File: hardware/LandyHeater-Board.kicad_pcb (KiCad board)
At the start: 4 copper layers, 98 x 48 mm, 0 parts

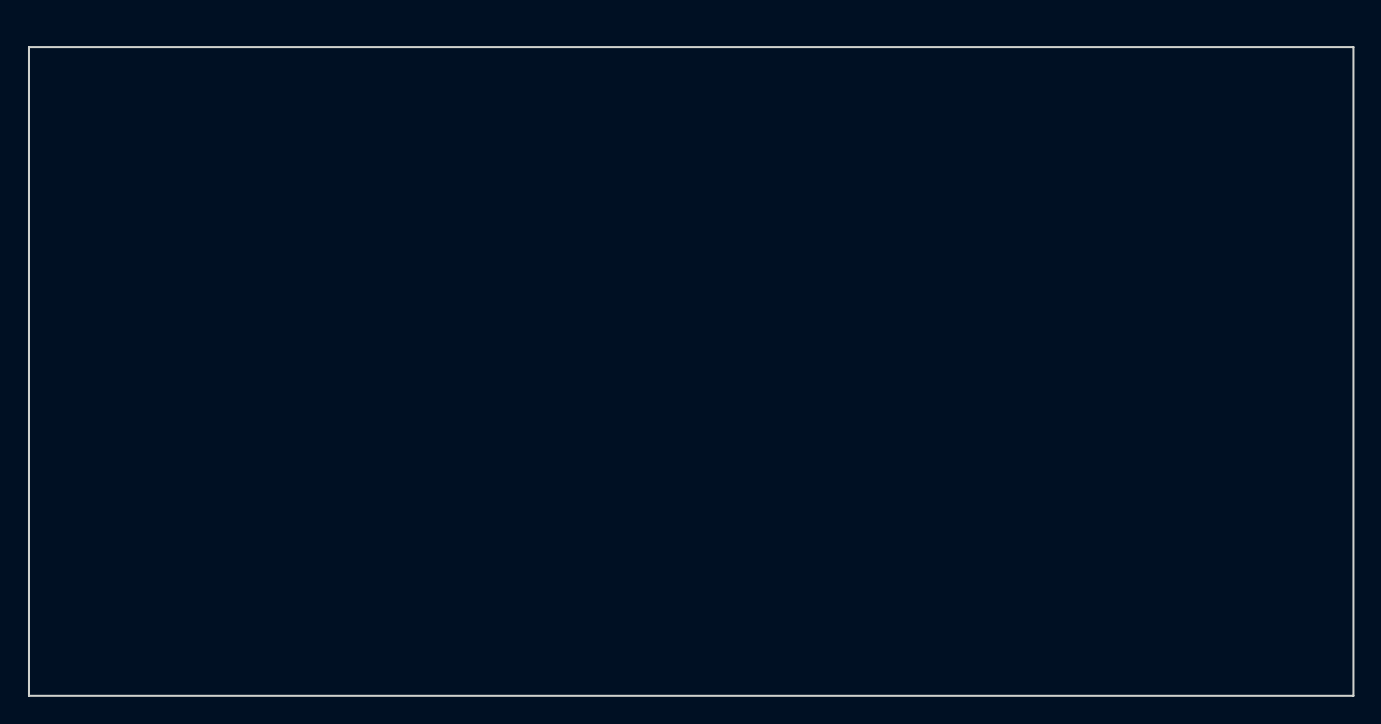
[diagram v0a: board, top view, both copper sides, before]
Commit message: Place Rev A board: 4-layer stackup, zones, two-sided placement
Generated by scripts/rebuild/gen_pcb.py from the same circuit definition.
Pre-route DRC: 0 errors, schematic parity: 0 issues.

Co-Authored-By: Claude Opus 5.5 <noreply@anthropic.com>
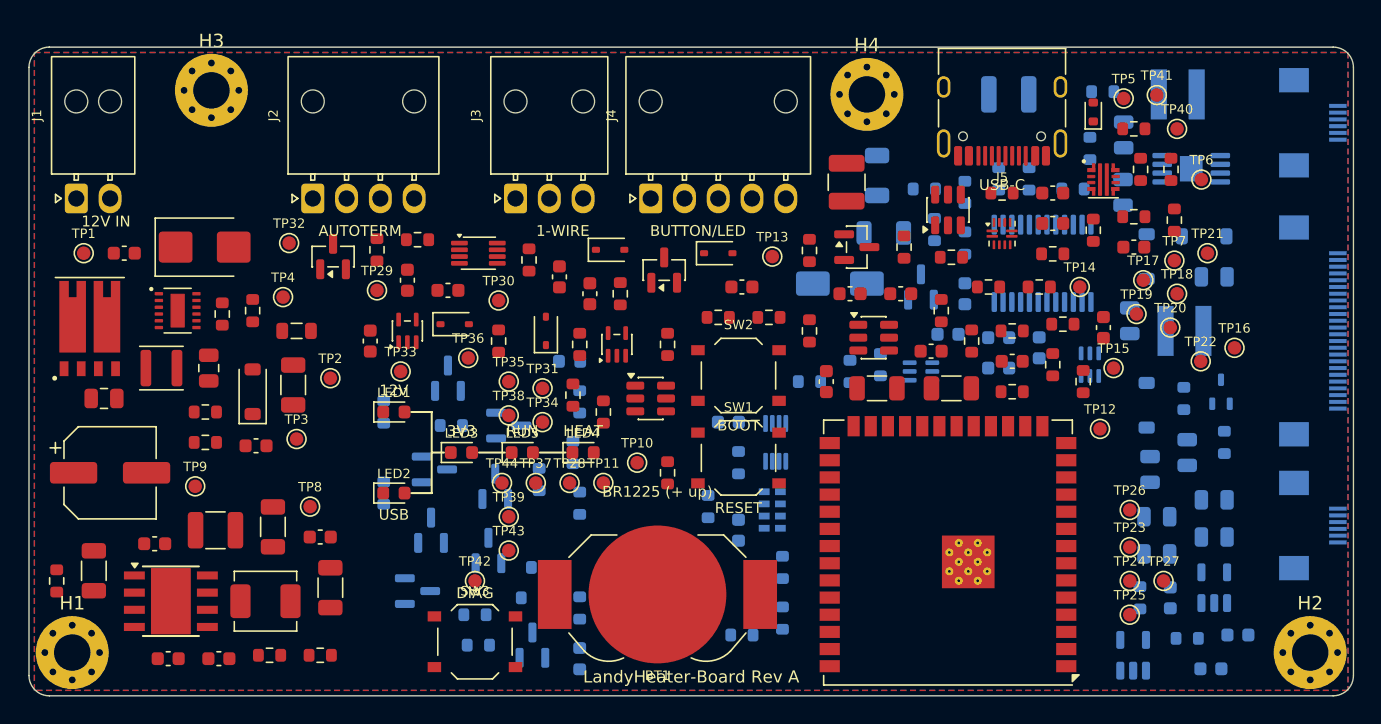
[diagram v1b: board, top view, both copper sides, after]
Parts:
- added BT1: BR1225, Battery:BatteryHolder_LINX_BAT-HLD-012-SMT, F.Cu at (146.5, 140.5)
- added C1: 100nF 50V X7R, Capacitor_SMD:C_0603_1608Metric, F.Cu at (107.0, 115.2)
- added C10: 4.7µF 50V X7R, Capacitor_SMD:C_1210_3225Metric, F.Cu at (113.8, 135.8)
- added C11: 4.7µF 50V X7R, Capacitor_SMD:C_1206_3216Metric, F.Cu at (104.8, 138.8)
- added C12: 100nF 50V X7R, Capacitor_SMD:C_0603_1608Metric, F.Cu at (109.3, 136.8)
- added C13: 100nF 50V X7R, Capacitor_SMD:C_0603_1608Metric, F.Cu at (114.0, 145.2)
- added C14: 1µF 50V X5R, Capacitor_SMD:C_0603_1608Metric, F.Cu at (110.3, 145.2)
- added C15: CFF opt., Capacitor_SMD:C_0603_1608Metric, F.Cu at (121.5, 136.2)
- added C16: 22µF 10V X7R, Capacitor_SMD:C_1206_3216Metric, F.Cu at (118.0, 135.5)
- added C17: 22µF 10V X7R, Capacitor_SMD:C_1206_3216Metric, F.Cu at (122.3, 140.0)
- added C18: 22µF 10V X7R, Capacitor_SMD:C_1206_3216Metric, F.Cu at (162.8, 125.2)
- added C19: 22µF 10V X7R, Capacitor_SMD:C_1206_3216Metric, F.Cu at (168.2, 125.2)
- added C2: 1µF 50V X7R, Capacitor_SMD:C_0805_2012Metric, F.Cu at (105.5, 126.0)
- added C20: 100nF 50V X7R, Capacitor_SMD:C_0603_1608Metric, F.Cu at (159.0, 124.8)
- added C21: 100nF 50V X7R, Capacitor_SMD:C_0603_1608Metric, F.Cu at (166.8, 122.5)
- added C22: 1µF 50V X5R, Capacitor_SMD:C_0603_1608Metric, F.Cu at (172.8, 123.2)
- added C23: 10pF C0G, Capacitor_SMD:C_0603_1608Metric, F.Cu at (164.5, 118.2)
- added C24: 10pF C0G, Capacitor_SMD:C_0603_1608Metric, F.Cu at (160.8, 118.2)
- added C25: 10pF C0G, Capacitor_SMD:C_0603_1608Metric, F.Cu at (179.5, 120.8)
- added C26: 1µF 50V X5R, Capacitor_SMD:C_0603_1608Metric, B.Cu at (169.2, 118.2)
- added C27: 100nF 50V X7R, Capacitor_SMD:C_0603_1608Metric, B.Cu at (171.8, 121.5)
- added C28: 100nF 50V X7R, Capacitor_SMD:C_0603_1608Metric, B.Cu at (168.0, 121.2)
- added C29: 100nF 50V X7R, Capacitor_SMD:C_0603_1608Metric, B.Cu at (174.8, 122.2)
- added C3: 1µF 50V X7R, Capacitor_SMD:C_0805_2012Metric, F.Cu at (113.3, 123.8)
- added C30: 100nF 50V X7R, Capacitor_SMD:C_0603_1608Metric, B.Cu at (171.8, 123.8)
- added C31: 4.7µF 25V X5R, Capacitor_SMD:C_0805_2012Metric, B.Cu at (187.7, 117.0)
- added C32: 4.7µF 25V X5R, Capacitor_SMD:C_0805_2012Metric, B.Cu at (185.7, 130.0)
- added C33: 1µF 50V X7R, Capacitor_SMD:C_0805_2012Metric, B.Cu at (181.4, 120.2)
- added C34: 1µF 50V X7R, Capacitor_SMD:C_0805_2012Metric, B.Cu at (187.7, 133.5)
- added C35: 1µF 50V X7R, Capacitor_SMD:C_0805_2012Metric, B.Cu at (182.9, 131.2)
- added C36: 1µF 50V X7R, Capacitor_SMD:C_0805_2012Metric, B.Cu at (180.9, 110.8)
- added C37: 1µF 50V X7R, Capacitor_SMD:C_0805_2012Metric, B.Cu at (187.7, 136.2)
- added C38: 1µF 50V X7R, Capacitor_SMD:C_0805_2012Metric, B.Cu at (183.4, 134.8)
- added C39: 1µF 50V X7R, Capacitor_SMD:C_0805_2012Metric, B.Cu at (183.4, 137.5)
- added C4: 10nF 50V X7R, Capacitor_SMD:C_0603_1608Metric, F.Cu at (116.8, 129.5)
- added C40: 1µF 50V X7R, Capacitor_SMD:C_0805_2012Metric, B.Cu at (181.0, 106.5)
- added C41: 1µF 50V X5R, Capacitor_SMD:C_0603_1608Metric, B.Cu at (189.4, 143.5)
- added C42: 1µF 50V X5R, Capacitor_SMD:C_0603_1608Metric, B.Cu at (184.4, 140.8)
- added C43: 100nF 50V X7R, Capacitor_SMD:C_0603_1608Metric, B.Cu at (187.4, 146.0)
- added C44: 100nF 50V X7R, Capacitor_SMD:C_0603_1608Metric, B.Cu at (151.8, 127.8)
- added C45: 100nF 50V X7R, Capacitor_SMD:C_0603_1608Metric, B.Cu at (152.5, 135.8)
- added C46: 1µF 50V X5R, Capacitor_SMD:C_0603_1608Metric, F.Cu at (131.0, 118.0)
- added C47: 100nF 50V X7R, Capacitor_SMD:C_0603_1608Metric, F.Cu at (125.2, 121.8)
- added C48: 100nF 50V X7R, Capacitor_SMD:C_0603_1608Metric, F.Cu at (128.0, 117.2)
- added C49: 1µF 50V X5R, Capacitor_SMD:C_0603_1608Metric, F.Cu at (141.5, 118.2)
- added C5: 4.7µF 50V X7R, Capacitor_SMD:C_1206_3216Metric, F.Cu at (119.5, 125.0)
- added C50: 100nF 50V X7R, Capacitor_SMD:C_0603_1608Metric, F.Cu at (139.2, 117.0)
- added C51: 10nF 50V X7R, Capacitor_SMD:C_0603_1608Metric, F.Cu at (152.8, 117.8)
- added C52: 4.7µF 50V X7R, Capacitor_SMD:C_1210_3225Metric, B.Cu at (172.5, 103.5)
- added C53: 4.7µF 50V X7R, Capacitor_SMD:C_1206_3216Metric, B.Cu at (162.8, 109.5)
- added C6: 47µF 35V, Capacitor_SMD:CP_Elec_6.3x7.7, F.Cu at (106.0, 131.5)
- added C7: 1µF 50V X5R, Capacitor_SMD:C_0603_1608Metric, F.Cu at (175.8, 110.8)
- added C8: 100nF 50V X7R, Capacitor_SMD:C_0603_1608Metric, F.Cu at (175.8, 113.0)
- added C9: 10nF 50V X7R, Capacitor_SMD:C_0603_1608Metric, F.Cu at (181.8, 114.8)
- added D1: TPSMB36CA, Diode_SMD:D_SMB, F.Cu at (113.0, 114.8)
- added D10: PESD3V3S2UT, Package_TO_SOT_SMD:SOT-23, F.Cu at (147.0, 116.5)
- added D11: PESD3V3S1BA, Diode_SMD:D_SOD-323, F.Cu at (151.0, 115.2)
- added D12: PESD24VL1BA, Diode_SMD:D_SOD-323, F.Cu at (143.0, 115.0)
- added D13: PESD24VL1BA, Diode_SMD:D_SOD-323, F.Cu at (138.2, 121.0)
- added D14: B140Q, Diode_SMD:D_SMA, B.Cu at (160.0, 117.5)
- added D15: BAS116, Package_TO_SOT_SMD:SOT-23, B.Cu at (130.0, 131.2)
- added D16: BAS116, Package_TO_SOT_SMD:SOT-23, B.Cu at (129.8, 135.8)
- added D17: BAS116, Package_TO_SOT_SMD:SOT-23, B.Cu at (134.5, 132.5)
- added D18: BAS116, Package_TO_SOT_SMD:SOT-23, B.Cu at (135.5, 128.0)
- added D19: BAS116, Package_TO_SOT_SMD:SOT-23, B.Cu at (128.8, 140.2)
- added D2: 18V, Diode_SMD:D_SOD-123, F.Cu at (116.5, 125.5)
- added D3: ESD5Z5.0T1G, Diode_SMD:D_SOD-523, F.Cu at (178.8, 104.8)
- added D4: MBR0530, Diode_SMD:D_SOD-123, B.Cu at (186.9, 114.0)
- added D5: MBR0530, Diode_SMD:D_SOD-123, B.Cu at (182.7, 115.5)
- added D6: MBR0530, Diode_SMD:D_SOD-123, B.Cu at (182.7, 126.5)
- added D7: BAS116, Package_TO_SOT_SMD:SOT-23, B.Cu at (149.2, 138.2)
- added D8: PESD5V0S1BA, Diode_SMD:D_SOD-323, F.Cu at (131.5, 120.5)
- added D9: PESD5V0S2BT, Package_TO_SOT_SMD:SOT-23, F.Cu at (122.5, 115.5)
- added F1: 50mA PTC, Fuse:Fuse_1210_3225Metric, F.Cu at (160.5, 110.0)
- added FB1: 220Ω@100MHz, Inductor_SMD:L_0805_2012Metric, F.Cu at (119.8, 121.0)
- added H1: M2.5, MountingHole:MountingHole_2.7mm_M2.5_Pad_Via, F.Cu at (103.2, 144.8)
- added H2: M2.5, MountingHole:MountingHole_2.7mm_M2.5_Pad_Via, F.Cu at (194.8, 144.8)
- added H3: M2.5, MountingHole:MountingHole_2.7mm_M2.5_Pad_Via, F.Cu at (113.5, 103.2)
- added H4: M2.5, MountingHole:MountingHole_2.7mm_M2.5_Pad_Via, F.Cu at (162.0, 103.5)
- added J1: 12V IN, Connector_Molex:Molex_Nano-Fit_105313-xx02_1x02_P2.50mm_Horizontal, F.Cu at (103.5, 111.2)
- added J2: AUTOTERM, Connector_Molex:Molex_Nano-Fit_105313-xx04_1x04_P2.50mm_Horizontal, F.Cu at (121.0, 111.2)
- added J3: 1-WIRE, Connector_Molex:Molex_Nano-Fit_105313-xx03_1x03_P2.50mm_Horizontal, F.Cu at (136.0, 111.2)
- added J4: BUTTON+LED, Connector_Molex:Molex_Nano-Fit_105313-xx05_1x05_P2.50mm_Horizontal, F.Cu at (146.0, 111.2)
- added J5: USB-C, Connector_USB:USB_C_Receptacle_HRO_TYPE-C-31-M-12, F.Cu at (172.0, 104.0)
- added J6: E-PAPER 24p, Connector_FFC-FPC:Hirose_FH12-24S-0.5SH_1x24-1MP_P0.50mm_Horizontal, B.Cu at (195.0, 121.0)
- added J7: TOUCH 6p, Connector_FFC-FPC:Hirose_FH12-6S-0.5SH_1x06-1MP_P0.50mm_Horizontal, B.Cu at (195.0, 135.4)
- added J8: FRONTLIGHT 6p, Connector_FFC-FPC:Hirose_FH12-6S-0.5SH_1x06-1MP_P0.50mm_Horizontal, B.Cu at (195.0, 105.6)
- added L1: 100µH, Inductor_SMD:L_APV_ANR3015, F.Cu at (109.8, 123.8)
- added L2: 1.2µH, Inductor_SMD:L_Sunlord_MWSA0402S, F.Cu at (117.5, 141.0)
- added L3: 47µH, Inductor_SMD:L_Taiyo-Yuden_NR-40xx, B.Cu at (185.5, 121.0)
- added L4: 47µH, Inductor_SMD:L_Taiyo-Yuden_NR-40xx, B.Cu at (185.0, 103.5)
- added LED1: 12V red, LED_SMD:LED_0603_1608Metric, F.Cu at (127.0, 127.0)
- added LED2: USB red, LED_SMD:LED_0603_1608Metric, F.Cu at (127.0, 133.0)
- added LED3: 3V3 red, LED_SMD:LED_0603_1608Metric, F.Cu at (132.0, 130.0)
- added LED4: HEAT red, LED_SMD:LED_0603_1608Metric, F.Cu at (141.0, 130.0)
- added LED5: RUN red, LED_SMD:LED_0603_1608Metric, F.Cu at (136.5, 130.0)
- added LED6: STATUS1 red, LED_SMD:LED_0603_1608Metric, B.Cu at (140.8, 145.2)
- added LED7: STATUS2 red, LED_SMD:LED_0603_1608Metric, B.Cu at (140.0, 123.2)
- added Q1: BUK7K17-60E, LandyHeater_RevA:Nexperia_LFPAK56D_SOT1205, F.Cu at (104.5, 120.5)
- added Q2: 2N7002K, Package_TO_SOT_SMD:SOT-23, F.Cu at (161.2, 114.8)
- added Q3: 2N7002K, Package_TO_SOT_SMD:SOT-23, B.Cu at (166.0, 117.8)
- added Q4: Si1308EDL, Package_TO_SOT_SMD:SOT-323_SC-70, B.Cu at (188.2, 125.5)
- added Q5: BC857B, Package_TO_SOT_SMD:SOT-23, B.Cu at (137.2, 144.2)
- added Q6: 2N7002K, Package_TO_SOT_SMD:SOT-23, B.Cu at (134.0, 137.2)
- added Q7: 2N7002K, Package_TO_SOT_SMD:SOT-23, B.Cu at (131.0, 124.5)
- added R1: 100k, Resistor_SMD:R_0603_1608Metric, F.Cu at (114.3, 119.8)
- added R10: 100k, Resistor_SMD:R_0603_1608Metric, F.Cu at (157.8, 115.0)
- added R11: 105k, Resistor_SMD:R_0603_1608Metric, F.Cu at (182.2, 109.0)
- added R12: 10.7k, Resistor_SMD:R_0603_1608Metric, F.Cu at (181.8, 106.0)
- added R13: 30.1k, Resistor_SMD:R_0603_1608Metric, F.Cu at (184.5, 109.0)
- added R14: 3.32k, Resistor_SMD:R_0603_1608Metric, F.Cu at (181.8, 112.5)
- added R15: 100k, Resistor_SMD:R_0603_1608Metric, F.Cu at (184.8, 112.8)
- added R16: 100k, Resistor_SMD:R_0603_1608Metric, F.Cu at (117.8, 145.0)
- added R17: 43.2k, Resistor_SMD:R_0603_1608Metric, F.Cu at (121.5, 145.0)
- added R18: 100k, Resistor_SMD:R_0603_1608Metric, F.Cu at (102.0, 139.5)
- added R19: 10k, Resistor_SMD:R_0603_1608Metric, F.Cu at (172.8, 125.5)
- added R2: 7.15k, Resistor_SMD:R_0603_1608Metric, F.Cu at (116.5, 119.5)
- added R20: 10k, Resistor_SMD:R_0603_1608Metric, F.Cu at (157.8, 121.0)
- added R21: 10k, Resistor_SMD:R_0603_1608Metric, F.Cu at (154.8, 120.0)
- added R22: 22Ω, Resistor_SMD:R_0603_1608Metric, F.Cu at (171.0, 117.8)
- added R23: 22Ω, Resistor_SMD:R_0603_1608Metric, F.Cu at (174.8, 117.8)
- added R24: 499Ω, Resistor_SMD:R_0603_1608Metric, F.Cu at (147.2, 131.5)
- added R25: 33Ω, Resistor_SMD:R_0603_1608Metric, F.Cu at (175.8, 123.5)
- added R26: 33Ω, Resistor_SMD:R_0603_1608Metric, F.Cu at (172.8, 121.0)
- added R27: 33Ω, Resistor_SMD:R_0603_1608Metric, F.Cu at (169.8, 121.8)
- added R28: 33Ω, Resistor_SMD:R_0603_1608Metric, F.Cu at (176.5, 120.5)
- added R29: 33Ω, Resistor_SMD:R_0603_1608Metric, F.Cu at (167.5, 119.5)
- added R3: 0Ω, Resistor_SMD:R_0603_1608Metric, F.Cu at (113.0, 127.0)
- added R30: 33Ω, Resistor_SMD:R_0603_1608Metric, F.Cu at (178.0, 124.8)
- added R31: 100k, Resistor_SMD:R_0603_1608Metric, B.Cu at (163.0, 123.5)
- added R32: 100k, Resistor_SMD:R_0603_1608Metric, B.Cu at (177.2, 110.5)
- added R33: 100k, Resistor_SMD:R_0603_1608Metric, B.Cu at (169.2, 114.5)
- added R34: 100k, Resistor_SMD:R_0603_1608Metric, B.Cu at (174.0, 109.8)
- added R35: 100k, Resistor_SMD:R_0603_1608Metric, B.Cu at (171.8, 109.8)
- added R36: 100k, Resistor_SMD:R_0603_1608Metric, B.Cu at (169.2, 110.8)
- added R37: 100k, Resistor_SMD:R_0603_1608Metric, B.Cu at (167.0, 113.5)
- added R38: 100k, Resistor_SMD:R_0603_1608Metric, B.Cu at (166.2, 110.5)
- added R39: 1M 1%, Resistor_SMD:R_0603_1608Metric, B.Cu at (188.4, 129.2)
- added R4: 100Ω, Resistor_SMD:R_0603_1608Metric, F.Cu at (113.0, 129.2)
- added R40: 2.2Ω 1%, Resistor_SMD:R_0603_1608Metric, B.Cu at (185.4, 126.0)
- added R41: 4.7k, Resistor_SMD:R_0603_1608Metric, B.Cu at (182.2, 140.8)
- added R42: 4.7k, Resistor_SMD:R_0603_1608Metric, B.Cu at (185.7, 143.8)
- added R43: 100k, Resistor_SMD:R_0603_1608Metric, B.Cu at (155.8, 142.2)
- added R44: 10k, Resistor_SMD:R_0603_1608Metric, B.Cu at (160.8, 124.0)
- added R45: 100Ω, Resistor_SMD:R_0603_1608Metric, B.Cu at (155.8, 138.5)
- added R46: 10k, Resistor_SMD:R_0603_1608Metric, B.Cu at (153.5, 140.5)
- added R47: 10k, Resistor_SMD:R_0603_1608Metric, B.Cu at (152.8, 143.5)
- added R48: 100k, Resistor_SMD:R_0603_1608Metric, B.Cu at (152.5, 130.8)
- added R49: 100Ω, Resistor_SMD:R_0603_1608Metric, B.Cu at (157.8, 124.8)
- added R5: 0Ω, Resistor_SMD:R_0603_1608Metric, F.Cu at (172.0, 110.8)
- added R50: 0Ω, Resistor_SMD:R_0603_1608Metric, B.Cu at (150.2, 134.0)
- added R51: 100k, Resistor_SMD:R_0603_1608Metric, F.Cu at (134.8, 121.8)
- added R52: 100Ω, Resistor_SMD:R_0603_1608Metric, F.Cu at (128.8, 114.2)
- added R53: 100Ω, Resistor_SMD:R_0603_1608Metric, F.Cu at (125.8, 115.0)
- added R54: 100k, Resistor_SMD:R_0603_1608Metric, F.Cu at (143.8, 118.2)
- added R55: 4.7k, Resistor_SMD:R_0603_1608Metric, F.Cu at (137.0, 115.8)
- added R56: 0Ω, Resistor_SMD:R_0603_1608Metric, F.Cu at (140.8, 122.0)
- added R57: 1k, Resistor_SMD:R_0603_1608Metric, F.Cu at (147.2, 122.0)
- added R58: 10k, Resistor_SMD:R_0603_1608Metric, F.Cu at (151.0, 120.0)
- added R59: 100Ω, Resistor_SMD:R_0603_1608Metric, F.Cu at (142.5, 127.0)
- added R6: 910k 1%, Resistor_SMD:R_0603_1608Metric, F.Cu at (175.8, 115.3)
- added R60: 100k, Resistor_SMD:R_0603_1608Metric, F.Cu at (140.2, 125.8)
- added R61: 2.0Ω 1%, Resistor_SMD:R_1206_3216Metric, B.Cu at (163.2, 113.8)
- added R62: 4.7k, Resistor_SMD:R_0603_1608Metric, B.Cu at (179.4, 103.3)
- added R63: 0Ω, Resistor_SMD:R_0603_1608Metric, B.Cu at (178.5, 107.5)
- added R64: 100k, Resistor_SMD:R_0603_1608Metric, B.Cu at (133.0, 142.0)
- added R65: 47k, Resistor_SMD:R_0603_1608Metric, B.Cu at (133.2, 144.2)
- added R66: 47k, Resistor_SMD:R_0603_1608Metric, B.Cu at (137.2, 140.8)
- added R67: 100k, Resistor_SMD:R_0603_1608Metric, B.Cu at (138.0, 138.5)
- added R68: 12k, Resistor_SMD:R_0603_1608Metric, B.Cu at (126.2, 127.0)
- added R69: 3.3k, Resistor_SMD:R_0603_1608Metric, B.Cu at (126.2, 133.0)
- added R7: 220k, Resistor_SMD:R_0603_1608Metric, F.Cu at (168.2, 115.5)
- added R70: 1.2k, Resistor_SMD:R_0603_1608Metric, B.Cu at (131.2, 128.0)
- added R71: 3.3k, Resistor_SMD:R_0603_1608Metric, B.Cu at (140.2, 130.0)
- added R72: 1.2k, Resistor_SMD:R_0603_1608Metric, B.Cu at (137.8, 132.0)
- added R73: 100k, Resistor_SMD:R_0603_1608Metric, B.Cu at (140.8, 133.8)
- added R74: 2.7k, Resistor_SMD:R_0603_1608Metric, B.Cu at (140.8, 141.5)
- added R75: 2.7k, Resistor_SMD:R_0603_1608Metric, B.Cu at (140.8, 126.2)
- added R8: 220k, Resistor_SMD:R_0603_1608Metric, F.Cu at (178.8, 113.5)
- added R9: 1M, Resistor_SMD:R_0603_1608Metric, F.Cu at (164.8, 114.8)
- added SW1: RESET, Button_Switch_SMD:SW_Push_1P1T_XKB_TS-1187A, F.Cu at (152.5, 130.4)
- added SW2: BOOT, Button_Switch_SMD:SW_Push_1P1T_XKB_TS-1187A, F.Cu at (152.5, 124.3)
- added SW3: DIAG, Button_Switch_SMD:SW_Push_1P1T_XKB_TS-1187A, F.Cu at (133.0, 144.0)
- added TP1: BATT_12V, TestPoint:TestPoint_Pad_D1.0mm, F.Cu at (104.0, 115.2)
- added TP10: U0TXD, TestPoint:TestPoint_Pad_D1.0mm, F.Cu at (145.0, 130.8)
- added TP11: U0RXD, TestPoint:TestPoint_Pad_D1.0mm, F.Cu at (142.5, 132.2)
- added TP12: CHIP_PU, TestPoint:TestPoint_Pad_D1.0mm, F.Cu at (179.2, 128.2)
- added TP13: BOOT, TestPoint:TestPoint_Pad_D1.0mm, F.Cu at (155.0, 115.5)
- added TP14: USB_D-, TestPoint:TestPoint_Pad_D1.0mm, F.Cu at (177.8, 117.8)
- added TP15: USB_D+, TestPoint:TestPoint_Pad_D1.0mm, F.Cu at (180.2, 123.8)
- added TP16: EPD_3V3, TestPoint:TestPoint_Pad_D1.0mm, F.Cu at (189.2, 122.2)
- added TP17: EPD_SCLK, TestPoint:TestPoint_Pad_D1.0mm, F.Cu at (182.4, 117.2)
- added TP18: EPD_MOSI, TestPoint:TestPoint_Pad_D1.0mm, F.Cu at (184.9, 118.2)
- added TP19: EPD_CS, TestPoint:TestPoint_Pad_D1.0mm, F.Cu at (181.9, 119.8)
- added TP2: 12V_PROT, TestPoint:TestPoint_Pad_D1.0mm, F.Cu at (122.3, 124.5)
- added TP20: EPD_DC, TestPoint:TestPoint_Pad_D1.0mm, F.Cu at (184.4, 120.8)
- added TP21: EPD_RST, TestPoint:TestPoint_Pad_D1.0mm, F.Cu at (187.2, 115.2)
- added TP22: EPD_BUSY, TestPoint:TestPoint_Pad_D1.0mm, F.Cu at (186.7, 123.2)
- added TP23: I2C_SDA, TestPoint:TestPoint_Pad_D1.0mm, F.Cu at (181.4, 137.0)
- added TP24: I2C_SCL, TestPoint:TestPoint_Pad_D1.0mm, F.Cu at (181.4, 139.5)
- added TP25: TOUCH_INT, TestPoint:TestPoint_Pad_D1.0mm, F.Cu at (181.4, 142.0)
- added TP26: TOUCH_RST, TestPoint:TestPoint_Pad_D1.0mm, F.Cu at (181.4, 134.2)
- added TP27: 3V0_AON, TestPoint:TestPoint_Pad_D1.0mm, F.Cu at (183.9, 139.5)
- added TP28: RTC_INT, TestPoint:TestPoint_Pad_D1.0mm, F.Cu at (140.0, 132.2)
- added TP29: AT_5V, TestPoint:TestPoint_Pad_D1.0mm, F.Cu at (125.8, 118.0)
- added TP3: VIN_SYS, TestPoint:TestPoint_Pad_D1.0mm, F.Cu at (119.8, 129.0)
- added TP30: AT_TX_3V3, TestPoint:TestPoint_Pad_D1.0mm, F.Cu at (134.8, 118.8)
- added TP31: AT_RX_3V3, TestPoint:TestPoint_Pad_D1.0mm, F.Cu at (138.0, 125.2)
- added TP32: AT_TX_5V, TestPoint:TestPoint_Pad_D1.0mm, F.Cu at (119.2, 114.5)
- added TP33: AT_RX_5V, TestPoint:TestPoint_Pad_D1.0mm, F.Cu at (127.5, 124.0)
- added TP34: AT_OE, TestPoint:TestPoint_Pad_D1.0mm, F.Cu at (138.0, 127.8)
- added TP35: 1WIRE, TestPoint:TestPoint_Pad_D1.0mm, F.Cu at (135.5, 124.8)
- added TP36: 3V3_SENS, TestPoint:TestPoint_Pad_D1.0mm, F.Cu at (132.5, 123.0)
- added TP37: SENSOR_EN, TestPoint:TestPoint_Pad_D1.0mm, F.Cu at (137.5, 132.2)
- added TP38: BUTTON, TestPoint:TestPoint_Pad_D1.0mm, F.Cu at (135.5, 127.2)
- added TP39: BTN_PWM, TestPoint:TestPoint_Pad_D1.0mm, F.Cu at (135.5, 134.8)
- added TP4: GND, TestPoint:TestPoint_Pad_D1.0mm, F.Cu at (118.8, 118.5)
- added TP40: FL_ISENSE, TestPoint:TestPoint_Pad_D1.0mm, F.Cu at (184.9, 106.0)
- added TP41: FL_PWM, TestPoint:TestPoint_Pad_D1.0mm, F.Cu at (183.4, 103.5)
- added TP42: DIAG, TestPoint:TestPoint_Pad_D1.0mm, F.Cu at (133.0, 139.5)
- added TP43: DIAG_GND, TestPoint:TestPoint_Pad_D1.0mm, F.Cu at (135.5, 137.2)
- added TP44: RUN, TestPoint:TestPoint_Pad_D1.0mm, F.Cu at (135.0, 132.2)
- added TP5: USB_VBUS, TestPoint:TestPoint_Pad_D1.0mm, F.Cu at (181.0, 103.8)
- added TP6: USB_FLT, TestPoint:TestPoint_Pad_D1.0mm, F.Cu at (186.8, 109.8)
- added TP7: USB_3A, TestPoint:TestPoint_Pad_D1.0mm, F.Cu at (184.8, 115.8)
- added TP8: 3V3, TestPoint:TestPoint_Pad_D1.0mm, F.Cu at (120.8, 134.0)
- added TP9: BUCK_PG, TestPoint:TestPoint_Pad_D1.0mm, F.Cu at (112.3, 132.5)
- added U1: LM74720QDRRRQ1, LandyHeater_RevA:TI_DRR0012F_WSON-12_3x3mm_RTN-float, F.Cu at (111.0, 119.5)
- added U10: SN74AXC1T45DCKR, Package_TO_SOT_SMD:SOT-363_SC-70-6, B.Cu at (178.5, 123.5)
- added U11: TPS7A0230PDBVR, Package_TO_SOT_SMD:SOT-23-5, B.Cu at (187.7, 140.0)
- added U12: 74LVC1G07, Package_TO_SOT_SMD:SOT-23-5, B.Cu at (181.7, 145.0)
- added U13: 74LVC1G74, Package_SO:VSSOP-8_2.3x2mm_P0.5mm, B.Cu at (155.2, 129.2)
- added U14: RV-3028-C7, LandyHeater_RevA:MicroCrystal_RV-3028-C7, B.Cu at (155.0, 134.2)
- added U15: TPS22945DCKR, Package_TO_SOT_SMD:SOT-353_SC-70-5, F.Cu at (128.0, 121.0)
- added U16: TXU0202QDCURQ1, Package_SO:VSSOP-8_2.3x2mm_P0.5mm, F.Cu at (133.2, 115.2)
- added U17: TPS22945DCKR, Package_TO_SOT_SMD:SOT-353_SC-70-5, F.Cu at (143.5, 122.0)
- added U18: BCR421UW6, Package_TO_SOT_SMD:SOT-23-6, F.Cu at (146.0, 126.0)
- added U19: AL8861QMP-13, Package_SO:MSOP-8-1EP_3x3mm_P0.65mm_EP1.68x1.88mm, B.Cu at (186.0, 109.0)
- added U2: USBLC6-2SC6, Package_TO_SOT_SMD:SOT-23-6, F.Cu at (168.0, 112.0)
- added U3: TUSB321AIRWBR, Package_DFN_QFN:Texas_X2QFN-12_1.6x1.6mm_P0.4mm, F.Cu at (172.0, 113.8)
- added U4: TPS259470LRPWR, LandyHeater_RevA:TI_RPW0010A_VQFN-HR-10_2x2mm, F.Cu at (179.5, 109.8)
- added U5: LMR33630CDDAR, Package_SO:Texas_HSOP-8-1EP_3.9x4.9mm_P1.27mm, F.Cu at (110.5, 141.0)
- added U6: ESP32-S3-WROOM-1U-N16R8, RF_Module:ESP32-S3-WROOM-1U, F.Cu at (168.0, 137.4)
- added U7: TPS3808G33-Q1, Package_TO_SOT_SMD:SOT-23-6, F.Cu at (162.5, 121.5)
- added U8: TPS22919DCKR, Package_TO_SOT_SMD:SOT-363_SC-70-6, B.Cu at (166.0, 124.0)
- added U9: SN74AXC8T245PWR, Package_SO:TSSOP-24_4.4x7.8mm_P0.65mm, B.Cu at (175.0, 116.0)
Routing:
- added copper zone on B.Cu, net GND
- added copper zone on F.Cu, net GND
- added copper zone on In1.Cu, net GND
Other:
- outline, holes or cut-outs redrawn
- rule pad_to_mask_clearance: 0 -> 0.05
- board text added: "1-WIRE"
- board text added: "12V"
- board text added: "12V IN"
- board text added: "3V3"
- board text added: "AUTOTERM"
- board text added: "BOOT"
- board text added: "BR1225 (+ up)"
- board text added: "BUTTON/LED"
- board text added: "DIAG"
- board text added: "E-PAPER"
- board text added: "FRONTLIGHT"
- board text added: "GDEY029T94-FT01 outline 79 x 36.7"
- board text added: "HEAT"
- board text added: "LandyHeater Rev A – display side"
- board text added: "LandyHeater-Board Rev A"
- board text added: "RESET"
- board text added: "RUN"
- board text added: "TOUCH"
- board text added: "USB"
- board text added: "USB-C"
- board text removed: "PROVISIONAL 98 x 48 mm OUTLINE - FINALIZE IN PHASE 3"
